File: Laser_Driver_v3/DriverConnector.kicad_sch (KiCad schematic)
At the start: 1 part, among them J3 Conn_02x12_Counter_Clockwise

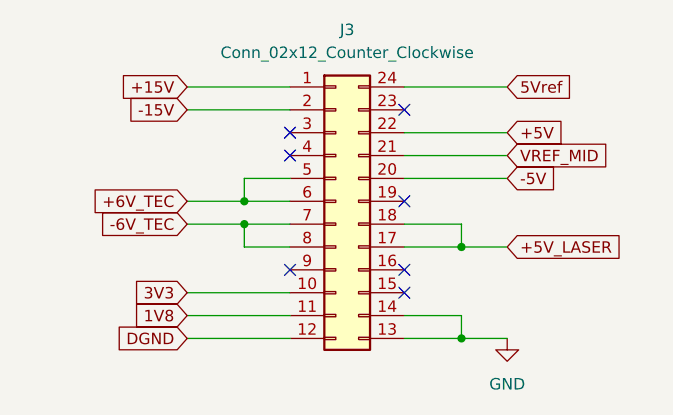
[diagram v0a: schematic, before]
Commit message: Added NTC for heatsink.  orrected screw terminal#s
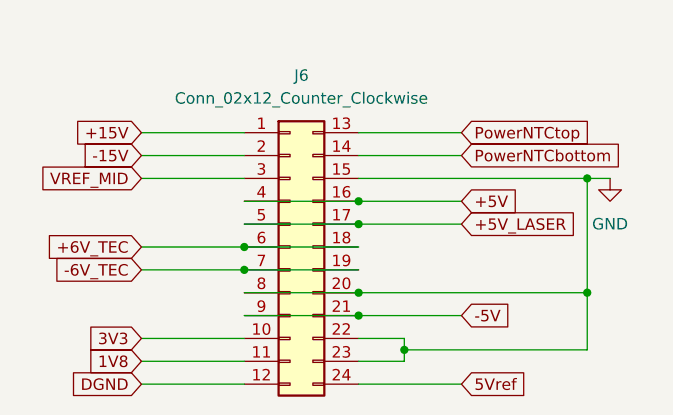
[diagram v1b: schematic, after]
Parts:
- removed J3: Conn_02x12_Counter_Clockwise, Connector_Molex:Molex_Micro-Fit_3.0_43045-2412_2x12_P3.00mm_Vertical, symbol Connector_Generic:Conn_02x12_Counter_Clockwise
- added J6: Conn_02x12_Counter_Clockwise, Connector_Molex:Molex_Micro-Fit_3.0_43045-2412_2x12_P3.00mm_Vertical, symbol Connector_Generic:Conn_02x12_Top_Bottom
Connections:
- net +15V: now also J6.1 (Pin_1)
- net +5V: now also J6.16 (Pin_16), J6.4 (Pin_4)
- net +5V_LASER: now also J6.17 (Pin_17), J6.5 (Pin_5)
- net +6V_TEC: now also J6.18 (Pin_18), J6.6 (Pin_6)
- net -15V: now also J6.2 (Pin_2)
- net -5V: now also J6.21 (Pin_21), J6.9 (Pin_9)
- net -6V_TEC: now also J6.19 (Pin_19), J6.7 (Pin_7)
- net 1V8: now also J6.11 (Pin_11)
- net 3V3: now also J6.10 (Pin_10)
- net 5Vref: now also J6.24 (Pin_24)
- net DGND: now also J6.12 (Pin_12)
- net GND: now also J6.15 (Pin_15), J6.20 (Pin_20), J6.22 (Pin_22), J6.23 (Pin_23), J6.8 (Pin_8)
- net VREF_MID: now also J6.3 (Pin_3)
- new net PowerNTCbottom: J6.14 (Pin_14)
- new net PowerNTCtop: J6.13 (Pin_13)
- no-connect marks 7 -> 0
